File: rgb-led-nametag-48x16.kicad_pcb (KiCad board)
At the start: 4 copper layers, 84 x 28.8 mm, 177 parts, among them J1 USB_C_Receptacle_USB2.0, Q1 CJ3139K, Q10 CJ3139K, Q11 CJ3139K, Q12 CJ3139K, Q13 CJ3139K, Q14 CJ3139K, Q15 CJ3139K, Q16 CJ3139K, Q17 CJ3139K, Q18 CJ3139K, Q19 2SK3541, Q2 CJ3139K, Q20 AO3401A, Q21 FS8205A, Q3 CJ3139K, Q4 CJ3139K, Q5 CJ3139K, Q6 CJ3139K, Q7 CJ3139K, Q8 CJ3139K, Q9 CJ3139K, SW1 SW_Push, SW2 SW_Push, U1 led-panel-16x16, U10 74HC595, U11 74HC595, U12 74HC595, U13 74HC595, U14 74HC595, U15 74HC595, U16 led-panel-16x16, U17 74HC595, U18 74HC595, U19 74HC595, U2 74HC595, U20 74HC595, U21 74HC595, U22 74HC595, U23 74HC595, U24 ESP32-PICO-D4, U25 STM32F722RETx, U26 SRV05-4, U27 TPS63001, U28 XC6206P332MR, U29 BQ24081, U3 74HC595, U30 DW01+G, U4 74HC595, U5 74HC595, U6 74HC595, U7 74HC595, U8 74HC595, U9 led-panel-16x16

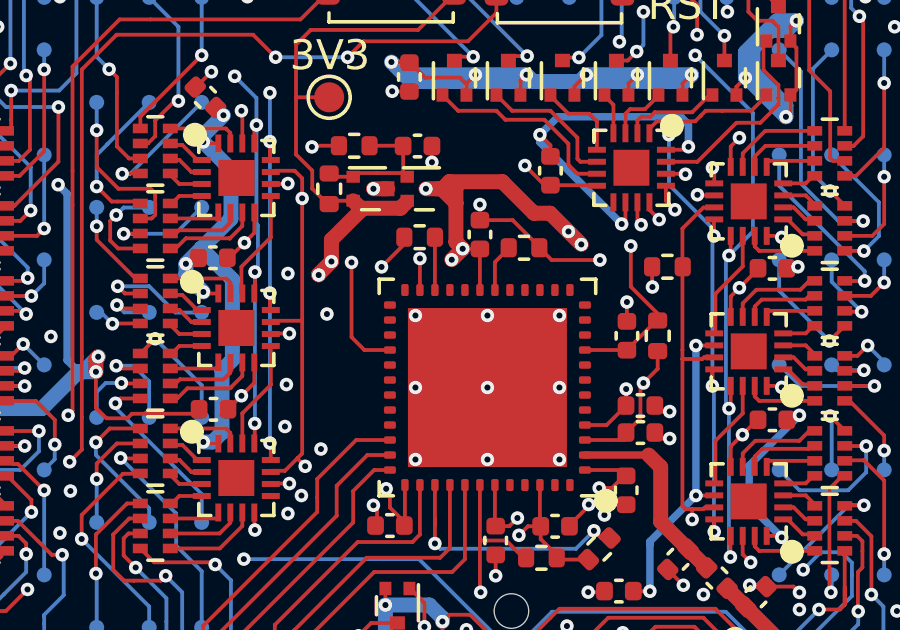
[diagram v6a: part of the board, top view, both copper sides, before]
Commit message: Improve ESP32 3V3 power routing
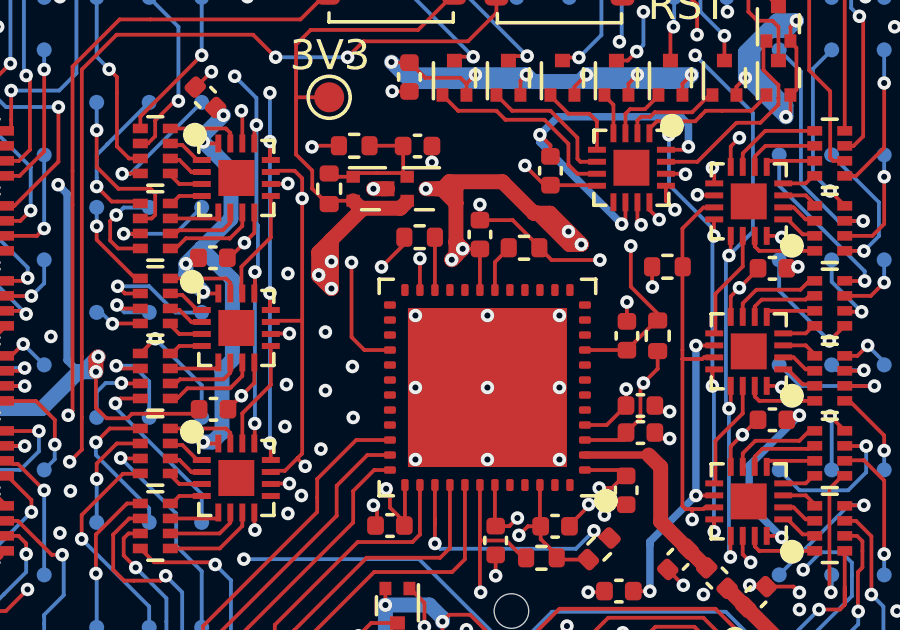
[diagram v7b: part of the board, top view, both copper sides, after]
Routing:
- net +3V3: track 155.6 -> 160.6 mm, vias 14 -> 15
- net /Sheet620161B9/3V3: track 65.3 -> 68.0 mm
- net /IRQ: track 57.2 -> 58.2 mm
- net GND: vias 139 -> 142
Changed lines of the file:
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@@
     (thickness 1.6)
     (drawings 45)
-    (tracks 4981)
+    (tracks 5004)
     (zones 0)
     (modules 177)
@@
   )
   (setup
-    (last_trace_width 0.127)
+    (last_trace_width 0.5)
     (user_trace_width 0.25)
     (user_trace_width 0.5)
@@
   (segment (start 163.03 106.065) (end 163.44 106.475) (width 0.127) (layer F.Cu) (net 2))
   (via (at 154.65 106.925) (size 0.45) (drill 0.2) (layers F.Cu B.Cu) (net 2))
-  (via (at 155.95 108.275) (size 0.45) (drill 0.2) (layers F.Cu B.Cu) (net 2))
   (via (at 155.75 112.775) (size 0.45) (drill 0.2) (layers F.Cu B.Cu) (net 2))
   (via (at 154.6 110.625) (size 0.45) (drill 0.2) (layers F.Cu B.Cu) (net 2))
@@
   (via (at 139.45 104.025) (size 0.45) (drill 0.2) (layers F.Cu B.Cu) (net 2))
   (via (at 139.975 103.775) (size 0.45) (drill 0.2) (layers F.Cu B.Cu) (net 2))
+  (via (at 155.9 108.875) (size 0.45) (drill 0.2) (layers F.Cu B.Cu) (net 2))
+  (via (at 155.9 110.825) (size 0.45) (drill 0.2) (layers F.Cu B.Cu) (net 2))
+  (via (at 156.825 111.725) (size 0.45) (drill 0.2) (layers F.Cu B.Cu) (net 2))
+  (via (at 156.8 110.025) (size 0.45) (drill 0.2) (layers F.Cu B.Cu) (net 2))
   (via (at 148.9 120.5) (size 0.45) (drill 0.2) (layers F.Cu B.Cu) (net 3))
   (segment (start 148.275 120.47) (end 148.87 120.47) (width 0.127) (layer B.Cu) (net 3))
@@
   (segment (start 164.55 112.475) (end 165.875 112.475) (width 0.127) (layer F.Cu) (net 372))
   (segment (start 164.55 111.975) (end 165.275 111.975) (width 0.127) (layer F.Cu) (net 372))
+  (segment (start 160.250001 106.324999) (end 160.11 106.465) (width 0.5) (layer F.Cu) (net 372))
+  (segment (start 160.250001 105.875001) (end 160.250001 106.324999) (width 0.5) (layer F.Cu) (net 372))
+  (segment (start 162.85 104.915) (end 162.99 104.915) (width 0.5) (layer F.Cu) (net 372))
+  (segment (start 164.03 105.955) (end 164.43 105.955) (width 0.5) (layer F.Cu) (net 372))
+  (segment (start 162.99 104.915) (end 164.03 105.955) (width 0.5) (layer F.Cu) (net 372))
   (segment (start 167.075 113.375) (end 166.675 112.975) (width 0.5) (layer F.Cu) (net 373))
   (segment (start 167.075 115.2) (end 167.075 113.375) (width 0.5) (layer F.Cu) (net 373))
@@
   (segment (start 153.89 105.035) (end 152.57 105.035) (width 0.5) (layer In1.Cu) (net 376))
   (segment (start 145.57 102.865) (end 145.28 103.155) (width 0.5) (layer In1.Cu) (net 376))
-  (segment (start 155.6525 106.7975) (end 153.89 105.035) (width 0.5) (layer In1.Cu) (net 376))
   (segment (start 155.8525 106.7975) (end 155.6525 106.7975) (width 0.5) (layer In1.Cu) (net 376))
   (segment (start 136.35 103.25) (end 136.445 103.155) (width 0.5) (layer In1.Cu) (net 376))
@@
   (segment (start 109.8 108.075) (end 109.825 108.05) (width 0.25) (layer In2.Cu) (net 376))
   (segment (start 106 108.075) (end 109.8 108.075) (width 0.25) (layer In2.Cu) (net 376))
+  (via (at 156.1 107.425) (size 0.45) (drill 0.2) (layers F.Cu B.Cu) (net 376))
+  (segment (start 156.1 106.525) (end 156.1 107.425) (width 0.5) (layer F.Cu) (net 376))
+  (segment (start 155.675 107) (end 156.1 107.425) (width 0.5) (layer F.Cu) (net 376))
+  (segment (start 155.675 106.975) (end 155.675 107) (width 0.5) (layer F.Cu) (net 376))
+  (segment (start 155.675 106.975) (end 155.675 107) (width 0.5) (layer In1.Cu) (net 376))
+  (segment (start 156.1 107.225) (end 156 107.325) (width 0.5) (layer In1.Cu) (net 376))
+  (segment (start 156.1 106.525) (end 156.1 107.225) (width 0.5) (layer In1.Cu) (net 376))
+  (segment (start 156 107.325) (end 156.1 107.425) (width 0.5) (layer In1.Cu) (net 376))
+  (segment (start 155.675 107) (end 156 107.325) (width 0.5) (layer In1.Cu) (net 376))
+  (segment (start 155.675 106.225) (end 156.1 105.8) (width 0.5) (layer F.Cu) (net 376))
+  (segment (start 155.675 106.975) (end 155.675 106.225) (width 0.5) (layer F.Cu) (net 376))
+  (segment (start 155.4275 106.5725) (end 153.89 105.035) (width 0.5) (layer In1.Cu) (net 376))
+  (segment (start 155.475 106.525) (end 155.4275 106.5725) (width 0.5) (layer In1.Cu) (net 376))
+  (segment (start 156.1 106.525) (end 155.475 106.525) (width 0.5) (layer In1.Cu) (net 376))
+  (segment (start 155.6525 106.7975) (end 155.4275 106.5725) (width 0.5) (layer In1.Cu) (net 376))
   (segment (start 96.88 96.46) (end 107.275 96.46) (width 0.5) (layer F.Cu) (net 377))
   (segment (start 107.275 96.46) (end 107.275 96.375) (width 0.5) (layer F.Cu) (net 377))
@@
   (segment (start 156.77 109.045) (end 156.77 106.555) (width 0.127) (layer F.Cu) (net 408))
   (segment (start 157.2 109.475) (end 156.77 109.045) (width 0.127) (layer F.Cu) (net 408))
-  (segment (start 155.24 108.085) (end 153.87 108.085) (width 0.127) (layer In2.Cu) (net 408))
   (segment (start 141.84 110.965) (end 141.274942 110.965) (width 0.127) (layer In2.Cu) (net 408))
   (segment (start 142.05 111.175) (end 141.84 110.965) (width 0.127) (layer In2.Cu) (net 408))
@@
   (segment (start 151.72 106.875) (end 151.35 107.245) (width 0.127) (layer In2.Cu) (net 408))
   (segment (start 151.06 107.245) (end 149.17 109.135) (width 0.127) (layer In2.Cu) (net 408))
-  (segment (start 153.87 108.085) (end 152.66 106.875) (width 0.127) (layer In2.Cu) (net 408))
   (segment (start 141.274942 110.965) (end 140.974942 111.265) (width 0.127) (layer In2.Cu) (net 408))
   (segment (start 149.17 109.135) (end 148.21 109.135) (width 0.127) (layer In2.Cu) (net 408))
-  (segment (start 152.66 106.875) (end 151.72 106.875) (width 0.127) (layer In2.Cu) (net 408))
   (segment (start 148.21 109.135) (end 146.17 111.175) (width 0.127) (layer In2.Cu) (net 408))
-  (segment (start 156.77 106.555) (end 155.24 108.085) (width 0.127) (layer In2.Cu) (net 408))
   (segment (start 140.974942 111.265) (end 139.72 111.265) (width 0.127) (layer In2.Cu) (net 408))
   (segment (start 138.75 110.295) (end 135.345 110.295) (width 0.127) (layer In2.Cu) (net 408))
@@
   (segment (start 123.9875 110.8125) (end 123.9 110.725) (width 0.127) (layer In2.Cu) (net 408))
   (segment (start 117.75 108.525) (end 111.275 108.525) (width 0.127) (layer In2.Cu) (net 408))
+  (segment (start 151.72 106.875) (end 152.175 106.875) (width 0.127) (layer In2.Cu) (net 408))
+  (segment (start 152.175 106.875) (end 153.675 108.375) (width 0.127) (layer In2.Cu) (net 408))
+  (segment (start 153.675 108.375) (end 156.375 108.375) (width 0.127) (layer In2.Cu) (net 408))
+  (segment (start 156.77 107.98) (end 156.77 106.555) (width 0.127) (layer In2.Cu) (net 408))
+  (segment (start 156.375 108.375) (end 156.77 107.98) (width 0.127) (layer In2.Cu) (net 408))
   (segment (start 157.85 113.475) (end 157.525 113.475) (width 0.127) (layer F.Cu) (net 409))
   (segment (start 157.525 113.475) (end 156.825 114.175) (width 0.127) (layer F.Cu) (net 409))

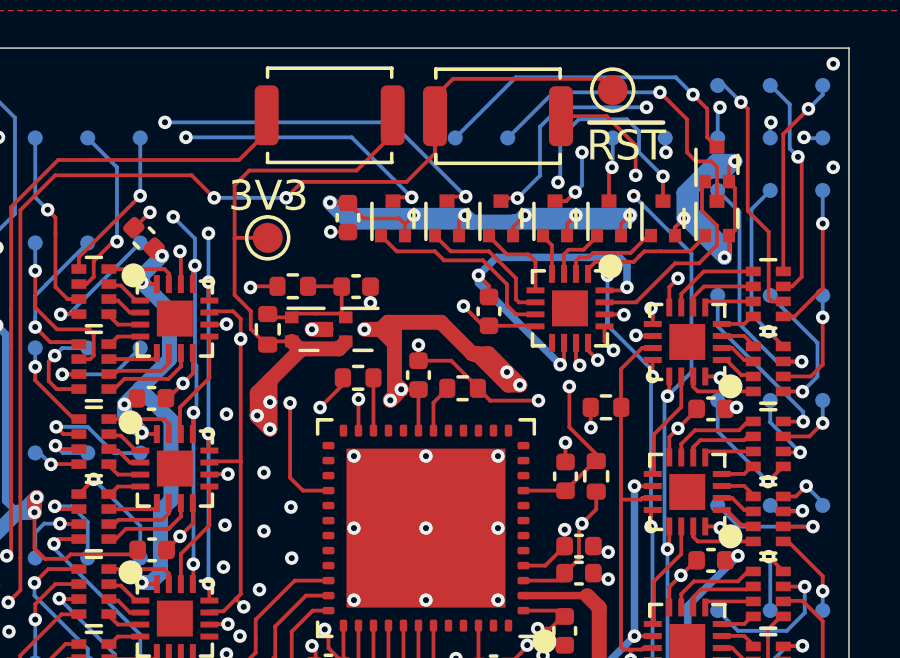
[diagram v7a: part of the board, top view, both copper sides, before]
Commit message: Improve VBUS impedance to high side drivers
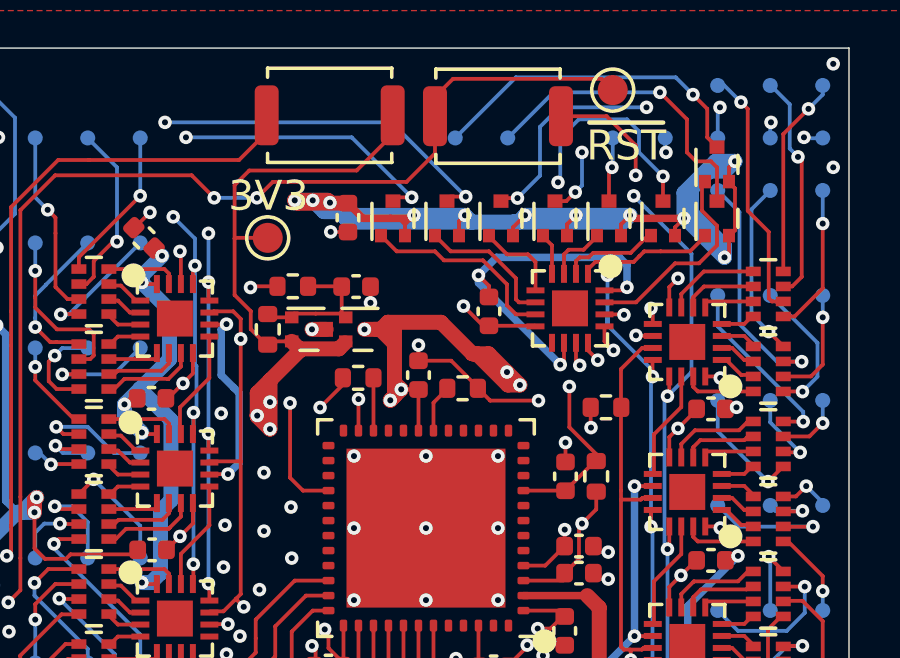
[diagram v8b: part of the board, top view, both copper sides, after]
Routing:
- net VBUS: track 444.8 -> 469.8 mm, vias 84 -> 86
- net /COL_~OE: track 199.8 -> 198.5 mm
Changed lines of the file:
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@@
     (thickness 1.6)
     (drawings 45)
-    (tracks 5004)
+    (tracks 5043)
     (zones 0)
     (modules 177)
@@
   )
   (setup
-    (last_trace_width 0.5)
+    (last_trace_width 0.25)
     (user_trace_width 0.25)
     (user_trace_width 0.5)
@@
   (segment (start 158.72 99.895) (end 159.225 100.4) (width 0.127) (layer F.Cu) (net 1))
   (segment (start 160.4 100.4) (end 160.6 100.6) (width 0.127) (layer F.Cu) (net 1))
-  (segment (start 159.225 100.4) (end 160.4 100.4) (width 0.127) (layer F.Cu) (net 1))
   (via (at 163 121.025) (size 0.45) (drill 0.2) (layers F.Cu B.Cu) (net 1))
   (segment (start 163.2 121.225) (end 163 121.025) (width 0.127) (layer F.Cu) (net 1))
@@
   (segment (start 157.9 117.975) (end 157.9 117.125) (width 0.5) (layer In1.Cu) (net 1))
   (segment (start 158.1 99.875) (end 157.725 99.875) (width 0.5) (layer In1.Cu) (net 1))
-  (segment (start 157.725 99.875) (end 155.9 101.7) (width 0.5) (layer In1.Cu) (net 1))
   (segment (start 155.9 101.7) (end 155.475 101.7) (width 0.5) (layer In1.Cu) (net 1))
   (segment (start 155.475 101.7) (end 154.8 102.375) (width 0.5) (layer In1.Cu) (net 1))
@@
   (segment (start 128.125 106.45) (end 128 106.575) (width 0.5) (layer B.Cu) (net 1))
   (segment (start 128.6 105.975) (end 128.125 106.45) (width 0.5) (layer B.Cu) (net 1))
+  (segment (start 168.2 100.4) (end 169.9 100.4) (width 0.25) (layer F.Cu) (net 1))
+  (segment (start 168.1 100.3) (end 168.2 100.4) (width 0.25) (layer F.Cu) (net 1))
+  (segment (start 171.6 98.7) (end 169.9 100.4) (width 0.5) (layer In2.Cu) (net 1))
+  (segment (start 171.6 98.5) (end 171.6 98.7) (width 0.5) (layer In2.Cu) (net 1))
+  (segment (start 171.2 101.7) (end 169.9 100.4) (width 0.5) (layer In2.Cu) (net 1))
+  (segment (start 171.25 101.7) (end 171.2 101.7) (width 0.5) (layer In2.Cu) (net 1))
+  (segment (start 168.2 100.4) (end 168.1 100.3) (width 0.5) (layer In2.Cu) (net 1))
+  (segment (start 169.9 100.4) (end 168.2 100.4) (width 0.5) (layer In2.Cu) (net 1))
+  (via (at 156.925 99.8) (size 0.45) (drill 0.2) (layers F.Cu B.Cu) (net 1))
+  (segment (start 157.02 99.895) (end 156.925 99.8) (width 0.5) (layer F.Cu) (net 1))
+  (segment (start 158.7 99.895) (end 157.02 99.895) (width 0.5) (layer F.Cu) (net 1))
+  (segment (start 158.025 99.8) (end 158.1 99.875) (width 0.5) (layer B.Cu) (net 1))
+  (segment (start 156.925 99.8) (end 158.025 99.8) (width 0.5) (layer B.Cu) (net 1))
+  (segment (start 158.025 99.8) (end 158.1 99.875) (width 0.5) (layer In1.Cu) (net 1))
+  (segment (start 156.925 99.8) (end 157.525 99.8) (width 0.5) (layer In1.Cu) (net 1))
+  (segment (start 156.925 99.8) (end 156.925 100.125) (width 0.5) (layer In1.Cu) (net 1))
+  (segment (start 157.2 100.4) (end 155.9 101.7) (width 0.5) (layer In1.Cu) (net 1))
+  (segment (start 156.925 100.125) (end 157.2 100.4) (width 0.5) (layer In1.Cu) (net 1))
+  (segment (start 157.725 99.875) (end 157.2 100.4) (width 0.5) (layer In1.Cu) (net 1))
+  (segment (start 158.025 99.8) (end 158.1 99.875) (width 0.5) (layer F.Cu) (net 1))
+  (segment (start 156.925 99.8) (end 158.025 99.8) (width 0.5) (layer F.Cu) (net 1))
+  (segment (start 158.7 99.9004) (end 159.1996 100.4) (width 0.25) (layer F.Cu) (net 1))
+  (segment (start 158.7 99.895) (end 158.7 99.9004) (width 0.25) (layer F.Cu) (net 1))
+  (segment (start 159.1996 100.4) (end 160.125 100.4) (width 0.25) (layer F.Cu) (net 1))
+  (segment (start 160.125 100.4) (end 160.4 100.4) (width 0.127) (layer F.Cu) (net 1))
+  (segment (start 159.225 100.4) (end 160.125 100.4) (width 0.127) (layer F.Cu) (net 1))
+  (segment (start 160.8 100.4) (end 160.9 100.3) (width 0.25) (layer F.Cu) (net 1))
+  (segment (start 160.125 100.4) (end 160.8 100.4) (width 0.25) (layer F.Cu) (net 1))
+  (segment (start 157.525 99.8) (end 158.025 99.8) (width 0.5) (layer In1.Cu) (net 1))
+  (via (at 157.525 99.8) (size 0.45) (drill 0.2) (layers F.Cu B.Cu) (net 1))
+  (segment (start 157 99.875) (end 156.925 99.8) (width 0.5) (layer B.Cu) (net 1))
+  (segment (start 158.1 99.875) (end 157 99.875) (width 0.5) (layer B.Cu) (net 1))
+  (segment (start 157.525 99.8) (end 157.9 100.175) (width 0.5) (layer B.Cu) (net 1))
+  (segment (start 158.4 100.175) (end 158.749999 100.524999) (width 0.5) (layer B.Cu) (net 1))
+  (segment (start 157.9 100.175) (end 158.4 100.175) (width 0.5) (layer B.Cu) (net 1))
+  (segment (start 154.65 103.925) (end 154.475 104.1) (width 0.25) (layer B.Cu) (net 1))
+  (segment (start 154.475 104.1) (end 154.475 105.625) (width 0.25) (layer B.Cu) (net 1))
+  (segment (start 154.8875 106.0375) (end 155.075 106.225) (width 0.25) (layer B.Cu) (net 1))
+  (segment (start 154.475 105.625) (end 154.8875 106.0375) (width 0.25) (layer B.Cu) (net 1))
+  (segment (start 155.075 108.55) (end 154.7 108.925) (width 0.25) (layer B.Cu) (net 1))
+  (segment (start 155.075 106.225) (end 155.075 108.55) (width 0.25) (layer B.Cu) (net 1))
   (via (at 158.9 108.325) (size 0.45) (drill 0.2) (layers F.Cu B.Cu) (net 2))
   (via (at 169.7 107.4) (size 0.45) (drill 0.2) (layers F.Cu B.Cu) (net 2))
@@
   (segment (start 163.44 106.475) (end 165.05 106.475) (width 0.127) (layer F.Cu) (net 2))
   (segment (start 163.03 106.065) (end 163.44 106.475) (width 0.127) (layer F.Cu) (net 2))
-  (via (at 154.65 106.925) (size 0.45) (drill 0.2) (layers F.Cu B.Cu) (net 2))
   (via (at 155.75 112.775) (size 0.45) (drill 0.2) (layers F.Cu B.Cu) (net 2))
   (via (at 154.6 110.625) (size 0.45) (drill 0.2) (layers F.Cu B.Cu) (net 2))
@@
   (via (at 156.825 111.725) (size 0.45) (drill 0.2) (layers F.Cu B.Cu) (net 2))
   (via (at 156.8 110.025) (size 0.45) (drill 0.2) (layers F.Cu B.Cu) (net 2))
+  (via (at 154.475 106.9) (size 0.45) (drill 0.2) (layers F.Cu B.Cu) (net 2))
   (via (at 148.9 120.5) (size 0.45) (drill 0.2) (layers F.Cu B.Cu) (net 3))
   (segment (start 148.275 120.47) (end 148.87 120.47) (width 0.127) (layer B.Cu) (net 3))
@@
   (segment (start 112.039411 117.885589) (end 112.75 117.175) (width 0.127) (layer F.Cu) (net 374))
   (segment (start 112.75 117.175) (end 112.775 117.175) (width 0.127) (layer F.Cu) (net 374))
-  (via (at 156.64 99.715) (size 0.45) (drill 0.2) (layers F.Cu B.Cu) (net 374))
   (via (at 154.24 99.715) (size 0.45) (drill 0.2) (layers F.Cu B.Cu) (net 374))
-  (segment (start 156.64 99.715) (end 154.24 99.715) (width 0.127) (layer B.Cu) (net 374))
   (segment (start 154.24 99.715) (end 153.49 98.965) (width 0.127) (layer F.Cu) (net 374))
   (segment (start 153.49 98.965) (end 148.94 98.965) (width 0.127) (layer F.Cu) (net 374))
@@
   (segment (start 161.6 96.995) (end 161.6 98.235) (width 0.127) (layer F.Cu) (net 374))
   (segment (start 161.6 98.235) (end 160.65 99.185) (width 0.127) (layer F.Cu) (net 374))
-  (segment (start 157.17 99.185) (end 156.64 99.715) (width 0.127) (layer F.Cu) (net 374))
   (segment (start 160.65 99.185) (end 157.17 99.185) (width 0.127) (layer F.Cu) (net 374))
   (via (at 147.375 113.2) (size 0.45) (drill 0.2) (layers F.Cu B.Cu) (net 374))
@@
   (segment (start 122.375 111.6) (end 120.5875 109.8125) (width 0.127) (layer In2.Cu) (net 374))
   (segment (start 120.1875 109.8125) (end 118.7125 109.8125) (width 0.127) (layer In2.Cu) (net 374))
+  (segment (start 156.195 99.185) (end 155.665 99.715) (width 0.127) (layer F.Cu) (net 374))
+  (via (at 155.665 99.715) (size 0.45) (drill 0.2) (layers F.Cu B.Cu) (net 374))
+  (segment (start 157.17 99.185) (end 156.195 99.185) (width 0.127) (layer F.Cu) (net 374))
+  (segment (start 155.665 99.715) (end 154.24 99.715) (width 0.127) (layer B.Cu) (net 374))
   (segment (start 110.143287 105.517625) (end 111.317956 104.342956) (width 0.127) (layer F.Cu) (net 375))
   (segment (start 114.032375 109.406713) (end 114.032375 109.417625) (width 0.127) (layer F.Cu) (net 376))
@@
   (segment (start 152.575 100.65) (end 146.725 100.65) (width 0.127) (layer In2.Cu) (net 381))
   (segment (start 159.875 100.925) (end 159.3 100.35) (width 0.127) (layer In2.Cu) (net 381))
-  (segment (start 168.525 100.925) (end 159.875 100.925) (width 0.127) (layer In2.Cu) (net 381))
-  (segment (start 168.7 100.75) (end 168.525 100.925) (width 0.127) (layer In2.Cu) (net 381))
-  (segment (start 168.7 100.125) (end 168.7 100.75) (width 0.127) (layer In2.Cu) (net 381))
   (segment (start 146.725 100.65) (end 145.825 101.55) (width 0.127) (layer In2.Cu) (net 381))
-  (segment (start 168.225 99.65) (end 168.7 100.125) (width 0.127) (layer In2.Cu) (net 381))
   (via (at 152.875 100.35) (size 0.45) (drill 0.2) (layers F.Cu B.Cu) (net 381))
   (segment (start 153.6 101.075) (end 152.875 100.35) (width 0.127) (layer B.Cu) (net 381))
@@
   (segment (start 114.225 106.825) (end 113.775 107.275) (width 0.127) (layer In2.Cu) (net 381))
   (segment (start 117.875 106.825) (end 115.025 106.825) (width 0.127) (layer In2.Cu) (net 381))
+  (segment (start 167.75 99.65) (end 166.475 100.925) (width 0.127) (layer In2.Cu) (net 381))
+  (segment (start 168.225 99.65) (end 167.75 99.65) (width 0.127) (layer In2.Cu) (net 381))
+  (segment (start 166.475 100.925) (end 159.875 100.925) (width 0.127) (layer In2.Cu) (net 381))
   (segment (start 116.95 114.5) (end 117.175 114.725) (width 0.127) (layer F.Cu) (net 382))
   (segment (start 117.175 114.725) (end 118.025 114.725) (width 0.127) (layer F.Cu) (net 382))
